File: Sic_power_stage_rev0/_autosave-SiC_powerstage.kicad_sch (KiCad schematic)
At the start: 34 parts, among them Q10 NTBG014N120M3P, Q11 NTBG014N120M3P, Q12 NTBG014N120M3P, Q7 NTBG014N120M3P, Q8 NTBG014N120M3P, Q9 NTBG014N120M3P

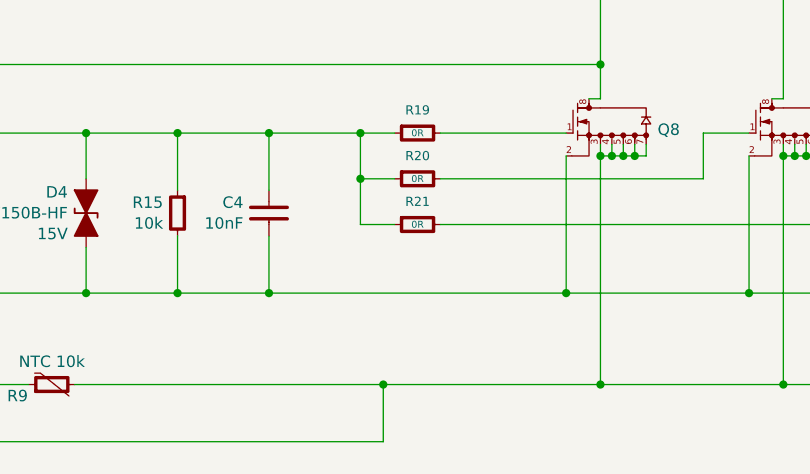
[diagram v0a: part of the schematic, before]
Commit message: WIP: define custom rules, change inner layer PWRGND , VBUS
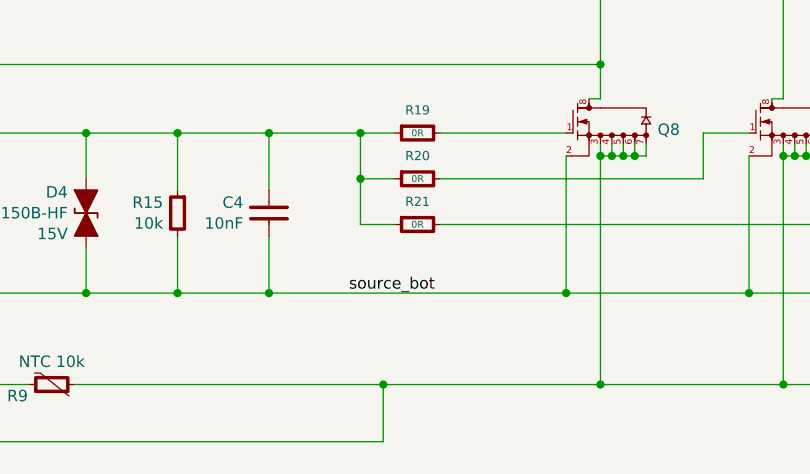
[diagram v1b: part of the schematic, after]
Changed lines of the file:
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@@
+		)
+	)
+	(label "source_bot"
+		(at 86.36 129.54 0)
+		(fields_autoplaced yes)
+		(effects
+			(font
+				(size 1.27 1.27)
+			)
+			(justify left bottom)
 		)
 	)
